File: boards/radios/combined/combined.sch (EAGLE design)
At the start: 16 parts

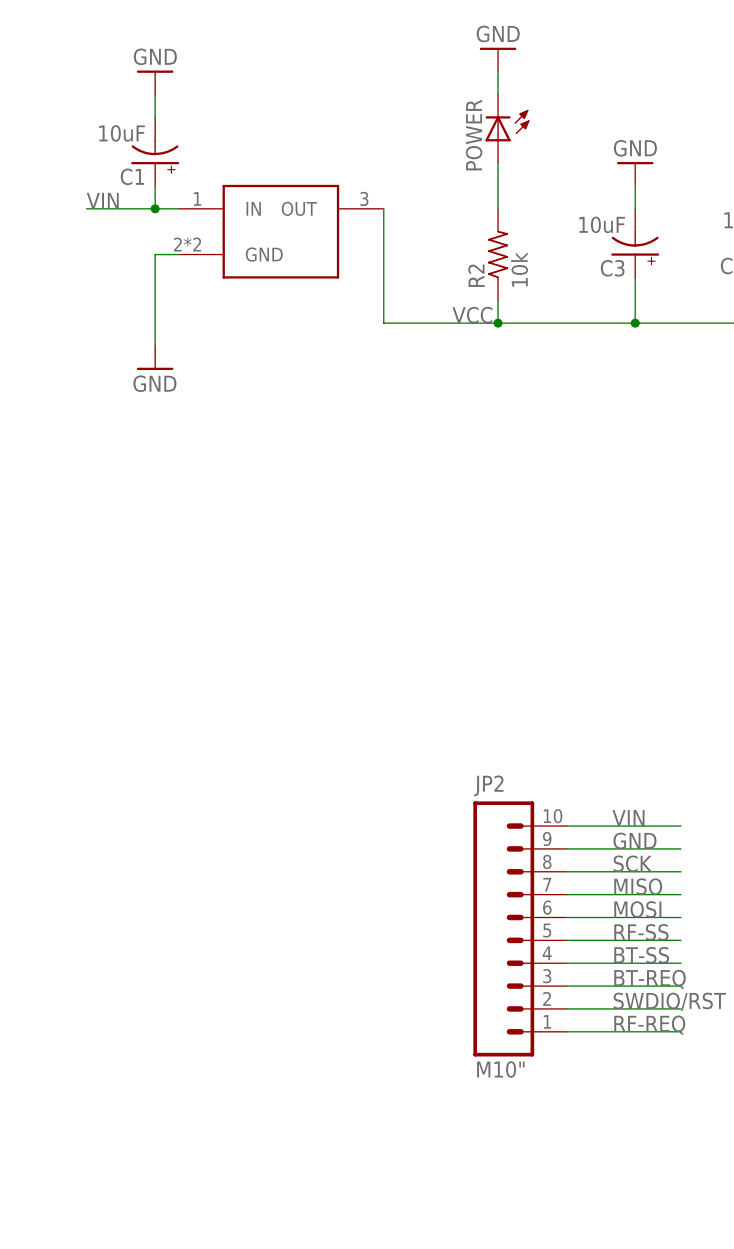
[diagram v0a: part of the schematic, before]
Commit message: updated radio with better regulator
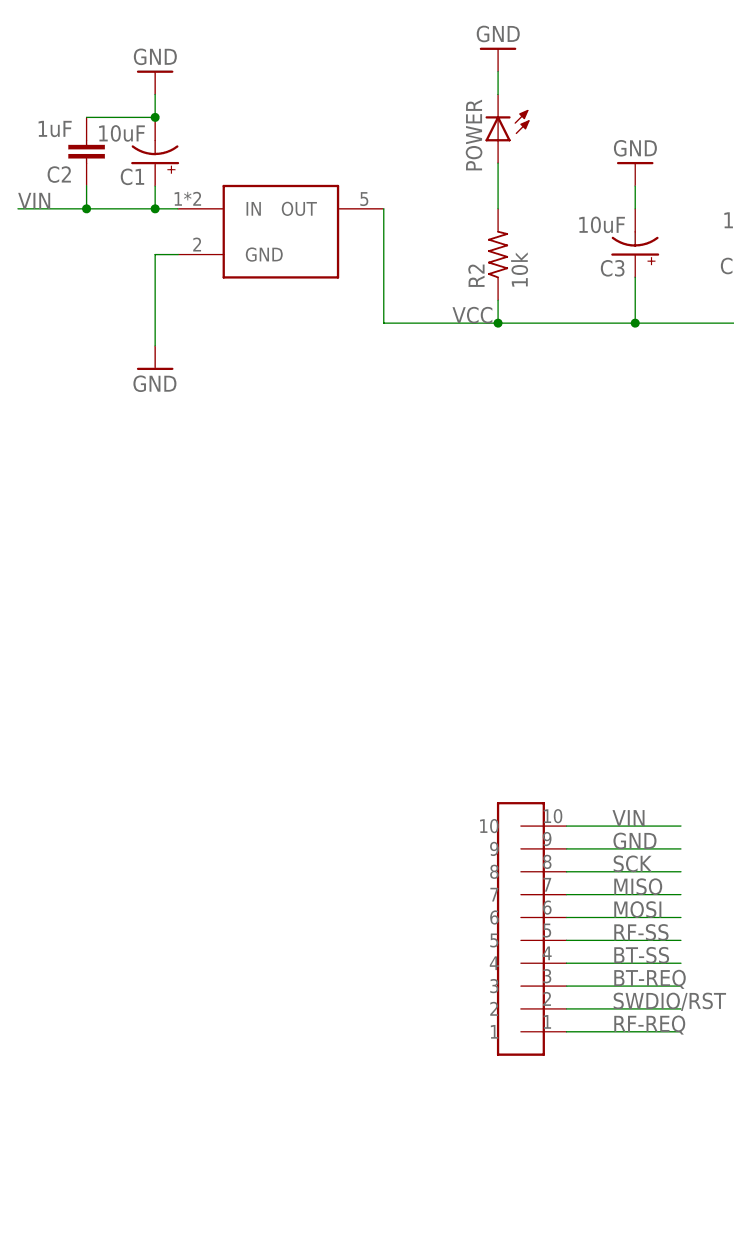
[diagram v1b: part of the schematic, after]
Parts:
- removed JP2: M10", SparkFun-Connectors:M10"
- added C2: 1uF, SparkFun:CAP0603-CAP
- added U$2: HEADER-10, homemade-hardware:HEADER-10
- U$3: value REGULATOR3.3V-UA78M33CDCYR -> REGULATOR3.3V-MIC5205; device ITP_Lab:REGULATOR3.3V-UA78M33CDCYR -> homemade-hardware:REGULATOR3.3V-MIC5205
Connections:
- net BT-REQ: now also U$2.3; no longer JP2.3
- net BT-SS: now also U$2.4; no longer JP2.4
- net GND: now also C2.2, U$2.9; no longer JP2.9
- net MISO: now also U$2.7; no longer JP2.7
- net MOSI: now also U$2.6; no longer JP2.6
- net RF-REQ: now also U$2.1; no longer JP2.1
- net RF-SS: now also U$2.5; no longer JP2.5
- net SCK: now also U$2.8; no longer JP2.8
- net SWDIO/RST: now also U$2.2; no longer JP2.2
- net VIN: now also C2.1, U$2.10; no longer JP2.10
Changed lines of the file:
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@@
 <part name="POWER" library="adafruit" deviceset="LED" device="CHIP-LED0603"/>
 <part name="GND2" library="SparkFun" deviceset="GND" device=""/>
-<part name="U$3" library="ITP_Lab" deviceset="REGULATOR" device="3.3V-UA78M33CDCYR"/>
 <part name="CLOCK" library="ITP_Lab" deviceset="PAD" device=""/>
 <part name="VCC" library="ITP_Lab" deviceset="PAD" device=""/>
@@
 <part name="GND4" library="SparkFun" deviceset="GND" device=""/>
 <part name="U$5" library="ITP_Lab" deviceset="NRF51-MDBT40-SPI" device=""/>
-<part name="JP2" library="SparkFun-Connectors" deviceset="M10" device="&quot;"/>
 <part name="CLOCK1" library="ITP_Lab" deviceset="PAD" device=""/>
+<part name="U$2" library="homemade-hardware" deviceset="HEADER-10" device=""/>
+<part name="U$3" library="homemade-hardware" deviceset="REGULATOR" device="3.3V-MIC5205"/>
+<part name="C2" library="SparkFun" deviceset="CAP" device="0603-CAP" value="1uF"/>
 </parts>
 <sheets>
@@
 <instance part="POWER" gate="G$1" x="91.44" y="223.52" rot="R180"/>
 <instance part="GND2" gate="1" x="91.44" y="233.68" rot="R180"/>
-<instance part="U$3" gate="G$1" x="66.04" y="215.9"/>
 <instance part="CLOCK" gate="G$1" x="254" y="152.4"/>
 <instance part="VCC" gate="G$1" x="254" y="137.16"/>
@@
 <instance part="GND4" gate="1" x="243.84" y="175.26" rot="R180"/>
 <instance part="U$5" gate="G$1" x="195.58" y="142.24"/>
-<instance part="JP2" gate="G$1" x="88.9" y="142.24"/>
 <instance part="CLOCK1" gate="G$1" x="236.22" y="149.86"/>
+<instance part="U$2" gate="G$1" x="93.98" y="124.46"/>
+<instance part="U$3" gate="G$1" x="66.04" y="215.9"/>
+<instance part="C2" gate="G$1" x="45.72" y="223.52" rot="R180"/>
 </instances>
 <busses>
@@
 <segment>
 <pinref part="GND6" gate="1" pin="GND"/>
-<pinref part="U$3" gate="G$1" pin="GND"/>
 <wire x1="53.34" y1="210.82" x2="53.34" y2="200.66" width="0.1524" layer="91"/>
 <wire x1="55.88" y1="210.82" x2="53.34" y2="210.82" width="0.1524" layer="91"/>
+<pinref part="U$3" gate="G$1" pin="GND"/>
 </segment>
 <segment>
@@
 <wire x1="99.06" y1="144.78" x2="111.76" y2="144.78" width="0.1524" layer="91"/>
 <label x="104.14" y="144.78" size="1.778" layer="95"/>
-<pinref part="JP2" gate="G$1" pin="9"/>
+<pinref part="U$2" gate="G$1" pin="9"/>
 </segment>
 <segment>
@@
 <pinref part="C1" gate="G$1" pin="-"/>
 <wire x1="53.34" y1="228.6" x2="53.34" y2="226.06" width="0.1524" layer="91"/>
+<pinref part="C2" gate="G$1" pin="2"/>
+<wire x1="45.72" y1="226.06" x2="53.34" y2="226.06" width="0.1524" layer="91"/>
+<junction x="53.34" y="226.06"/>
 </segment>
 <segment>
@@
 <wire x1="91.44" y1="205.74" x2="91.44" y2="203.2" width="0.1524" layer="91"/>
 <junction x="91.44" y="203.2"/>
+<wire x1="78.74" y1="203.2" x2="78.74" y2="215.9" width="0.1524" layer="91"/>
 <pinref part="U$3" gate="G$1" pin="OUT"/>
-<wire x1="78.74" y1="203.2" x2="78.74" y2="215.9" width="0.1524" layer="91"/>
 </segment>
 <segment>
@@
 <net name="VIN" class="0">
 <segment>
-<pinref part="U$3" gate="G$1" pin="IN"/>
-<label x="45.72" y="215.9" size="1.778" layer="95"/>
+<label x="38.1" y="215.9" size="1.778" layer="95"/>
 <wire x1="55.88" y1="215.9" x2="53.34" y2="215.9" width="0.1524" layer="91"/>
 <pinref part="C1" gate="G$1" pin="+"/>
 <wire x1="53.34" y1="215.9" x2="45.72" y2="215.9" width="0.1524" layer="91"/>
+<wire x1="45.72" y1="215.9" x2="38.1" y2="215.9" width="0.1524" layer="91"/>
 <wire x1="53.34" y1="215.9" x2="53.34" y2="218.44" width="0.1524" layer="91"/>
 <junction x="53.34" y="215.9"/>
+<pinref part="U$3" gate="G$1" pin="IN"/>
+<pinref part="C2" gate="G$1" pin="1"/>
+<wire x1="45.72" y1="218.44" x2="45.72" y2="215.9" width="0.1524" layer="91"/>
+<junction x="45.72" y="215.9"/>
 </segment>
 <segment>
 <wire x1="99.06" y1="147.32" x2="111.76" y2="147.32" width="0.1524" layer="91"/>
 <label x="104.14" y="147.32" size="1.778" layer="95"/>
-<pinref part="JP2" gate="G$1" pin="10"/>
+<pinref part="U$2" gate="G$1" pin="10"/>
 </segment>
 </net>
@@
 <wire x1="99.06" y1="124.46" x2="111.76" y2="124.46" width="0.1524" layer="91"/>
 <label x="104.14" y="124.46" size="1.778" layer="95"/>
-<pinref part="JP2" gate="G$1" pin="1"/>
+<pinref part="U$2" gate="G$1" pin="1"/>
 </segment>
 </net>
@@
 <wire x1="99.06" y1="134.62" x2="111.76" y2="134.62" width="0.1524" layer="91"/>
 <label x="104.14" y="134.62" size="1.778" layer="95"/>
-<pinref part="JP2" gate="G$1" pin="5"/>
+<pinref part="U$2" gate="G$1" pin="5"/>
 </segment>
 </net>
@@
 <wire x1="99.06" y1="127" x2="111.76" y2="127" width="0.1524" layer="91"/>
 <label x="104.14" y="127" size="1.778" layer="95"/>
-<pinref part="JP2" gate="G$1" pin="2"/>
+<pinref part="U$2" gate="G$1" pin="2"/>
 </segment>
 </net>
@@
 <wire x1="99.06" y1="137.16" x2="111.76" y2="137.16" width="0.1524" layer="91"/>
 <label x="104.14" y="137.16" size="1.778" layer="95"/>
-<pinref part="JP2" gate="G$1" pin="6"/>
+<pinref part="U$2" gate="G$1" pin="6"/>
 </segment>
 <segment>
@@
 <wire x1="99.06" y1="139.7" x2="111.76" y2="139.7" width="0.1524" layer="91"/>
 <label x="104.14" y="139.7" size="1.778" layer="95"/>
-<pinref part="JP2" gate="G$1" pin="7"/>
+<pinref part="U$2" gate="G$1" pin="7"/>
 </segment>
 <segment>
@@
 <wire x1="99.06" y1="142.24" x2="111.76" y2="142.24" width="0.1524" layer="91"/>
 <label x="104.14" y="142.24" size="1.778" layer="95"/>
-<pinref part="JP2" gate="G$1" pin="8"/>
+<pinref part="U$2" gate="G$1" pin="8"/>
 </segment>
 <segment>
@@
 <wire x1="99.06" y1="129.54" x2="111.76" y2="129.54" width="0.1524" layer="91"/>
 <label x="104.14" y="129.54" size="1.778" layer="95"/>
-<pinref part="JP2" gate="G$1" pin="3"/>
+<pinref part="U$2" gate="G$1" pin="3"/>
 </segment>
 </net>
@@
 <wire x1="99.06" y1="132.08" x2="111.76" y2="132.08" width="0.1524" layer="91"/>
 <label x="104.14" y="132.08" size="1.778" layer="95"/>
-<pinref part="JP2" gate="G$1" pin="4"/>
-</segment>
-</net>
+<pinref part="U$2" gate="G$1" pin="4"/>
+</segment>
+</net>
